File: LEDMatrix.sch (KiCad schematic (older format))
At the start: 71 parts

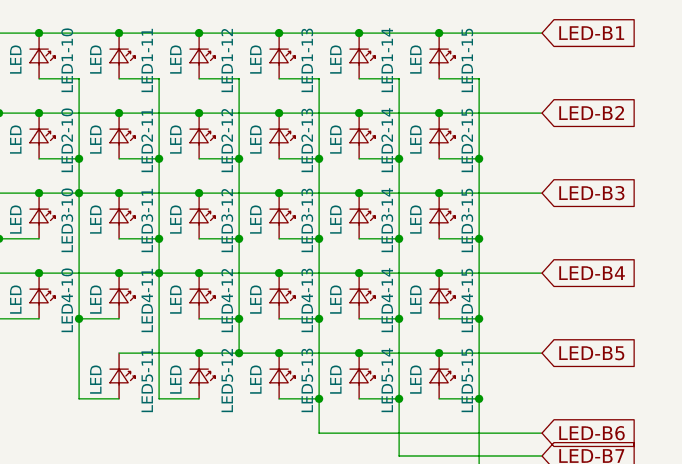
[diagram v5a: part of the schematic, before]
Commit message: Fix LED quantity for enter
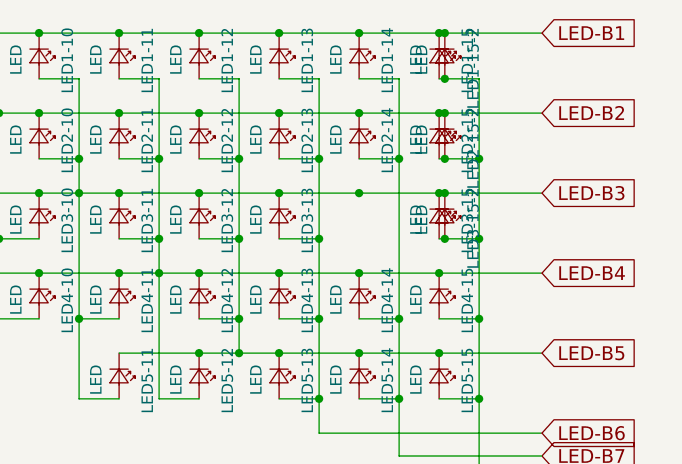
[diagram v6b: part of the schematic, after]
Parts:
- removed LED3-14: LED, MX_Alps_Hybrid:LED, symbol LED_Small
- added LED1-15-2, LED2-15-2, LED3-15-2: LED, MX_Alps_Hybrid:LED, symbol LED_Small
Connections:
- net LED-B1: now also LED1-15-2.1 (K)
- net LED-B2: now also LED2-15-2.1 (K)
- net LED-B3: now also LED3-15-2.1 (K)
- net LED-B8: now also LED1-15-2.2 (A), LED2-15-2.2 (A), LED3-15-2.2 (A)
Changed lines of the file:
@@
-$EndComp
-$Comp
-L LED_Small LED3-14
-U 1 1 5A6E13FF
-P 6950 2650
-F 0 "LED3-14" H 6825 2775 50  0000 L CNN
-F 1 "LED" H 6900 2550 50  0000 L CNN
-F 2 "MX_Alps_Hybrid:LED" V 6950 2650 50  0001 C CNN
-F 3 "" V 6950 2650 50  0001 C CNN
-	1    6950 2650
-	0    1    1    0
 $EndComp
 $Comp
@@
 Wire Wire Line
 	7125 2400 6950 2400
-Wire Wire Line
-	7125 2750 6950 2750
 Connection ~ 7125 2400
 Wire Wire Line
 	7125 3100 6950 3100
-Connection ~ 7125 2750
 Wire Wire Line
 	7125 3450 6950 3450
@@
 Connection ~ 4650 3250
 Connection ~ 4675 3450
+$Comp
+L LED_Small LED1-15-2
+U 1 1 5A6DC964
+P 7325 1950
+F 0 "LED1-15-2" H 7200 2075 50  0000 L CNN
+F 1 "LED" H 7275 1850 50  0000 L CNN
+F 2 "MX_Alps_Hybrid:LED" V 7325 1950 50  0001 C CNN
+F 3 "" V 7325 1950 50  0001 C CNN
+	1    7325 1950
+	0    1    1    0
+$EndComp
+Connection ~ 7325 1850
+Connection ~ 7325 2050
+$Comp
+L LED_Small LED2-15-2
+U 1 1 5A6DCCEC
+P 7325 2300
+F 0 "LED2-15-2" H 7200 2425 50  0000 L CNN
+F 1 "LED" H 7275 2200 50  0000 L CNN
+F 2 "MX_Alps_Hybrid:LED" V 7325 2300 50  0001 C CNN
+F 3 "" V 7325 2300 50  0001 C CNN
+	1    7325 2300
+	0    1    1    0
+$EndComp
+Connection ~ 7325 2200
+Connection ~ 7325 2400
+$Comp
+L LED_Small LED3-15-2
+U 1 1 5A6DD788
+P 7325 2650
+F 0 "LED3-15-2" H 7200 2775 50  0000 L CNN
+F 1 "LED" H 7275 2550 50  0000 L CNN
+F 2 "MX_Alps_Hybrid:LED" V 7325 2650 50  0001 C CNN
+F 3 "" V 7325 2650 50  0001 C CNN
+	1    7325 2650
+	0    1    1    0
+$EndComp
+Connection ~ 7325 2550
+Connection ~ 7325 2750
 $EndSCHEMATC

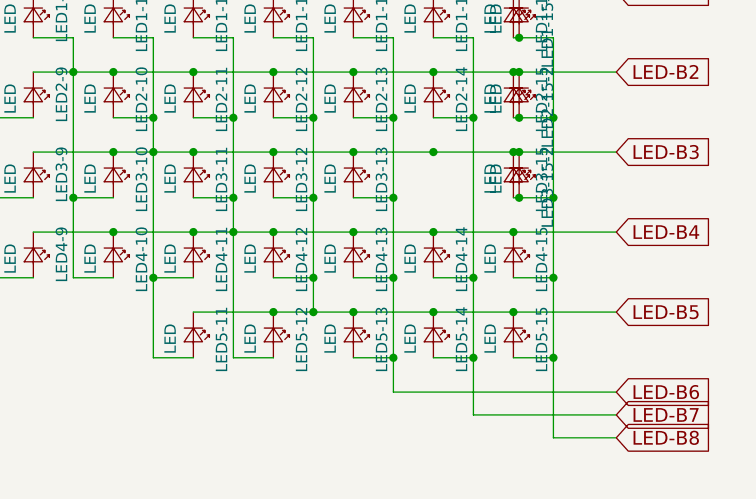
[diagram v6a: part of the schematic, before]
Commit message: Add missing shift-row footprints
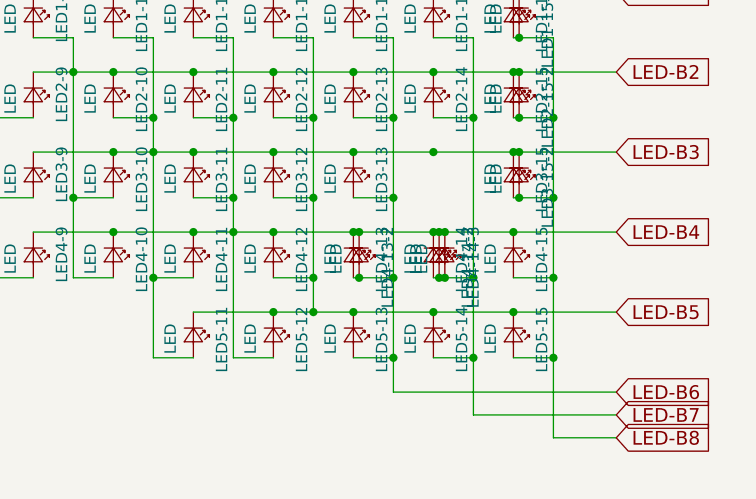
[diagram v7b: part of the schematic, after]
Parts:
- added LED4-13-2, LED4-14-2: LED, MX_Alps_Hybrid:LED, symbol LED_Small
- added LED4-14-3: LED, MX_Alps_Hybrid:LED-FLIPPED, symbol LED_Small
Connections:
- net LED-B4: now also LED4-13-2.1 (K), LED4-14-2.1 (K), LED4-14-3.1 (K)
- net LED-B6: now also LED4-13-2.2 (A)
- net LED-B7: now also LED4-14-2.2 (A), LED4-14-3.2 (A)
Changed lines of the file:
@@
 Connection ~ 7325 2550
 Connection ~ 7325 2750
+$Comp
+L LED_Small LED4-13-2
+U 1 1 5A6DE057
+P 6625 3000
+F 0 "LED4-13-2" H 6500 3125 50  0000 L CNN
+F 1 "LED" H 6575 2900 50  0000 L CNN
+F 2 "MX_Alps_Hybrid:LED" V 6625 3000 50  0001 C CNN
+F 3 "" V 6625 3000 50  0001 C CNN
+	1    6625 3000
+	0    1    1    0
+$EndComp
+Connection ~ 6625 2900
+Connection ~ 6625 3100
+$Comp
+L LED_Small LED4-14-2
+U 1 1 5A6DEC93
+P 6975 3000
+F 0 "LED4-14-2" H 6850 3125 50  0000 L CNN
+F 1 "LED" H 6925 2900 50  0000 L CNN
+F 2 "MX_Alps_Hybrid:LED" V 6975 3000 50  0001 C CNN
+F 3 "" V 6975 3000 50  0001 C CNN
+	1    6975 3000
+	0    1    1    0
+$EndComp
+$Comp
+L LED_Small LED4-14-3
+U 1 1 5A6DEEC6
+P 7000 3000
+F 0 "LED4-14-3" H 6875 3125 50  0000 L CNN
+F 1 "LED" H 6950 2900 50  0000 L CNN
+F 2 "MX_Alps_Hybrid:LED-FLIPPED" V 7000 3000 50  0001 C CNN
+F 3 "" V 7000 3000 50  0001 C CNN
+	1    7000 3000
+	0    1    1    0
+$EndComp
+Connection ~ 6975 2900
+Connection ~ 7000 2900
+Connection ~ 7000 3100
+Connection ~ 6975 3100
 $EndSCHEMATC

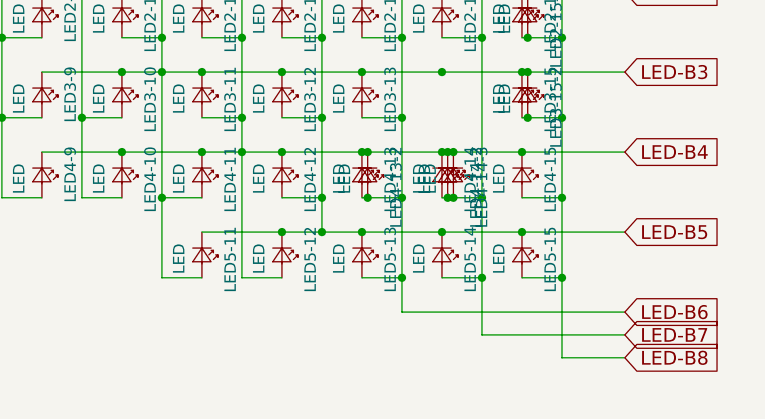
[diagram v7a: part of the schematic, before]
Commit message: Finish placing LEDs
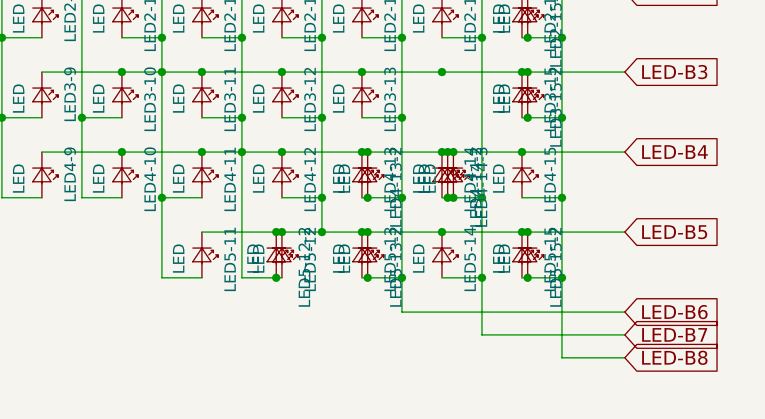
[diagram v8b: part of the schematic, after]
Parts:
- added LED5-12-2, LED5-15-2: LED, MX_Alps_Hybrid:LED-FLIPPED, symbol LED_Small
- added LED5-13-2: LED, MX_Alps_Hybrid:LED, symbol LED_Small
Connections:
- net LED-B4: now also LED5-12-2.2 (A)
- net LED-B5: now also LED5-12-2.1 (K), LED5-13-2.1 (K), LED5-15-2.1 (K)
- net LED-B6: now also LED5-13-2.2 (A)
- net LED-B8: now also LED5-15-2.2 (A)
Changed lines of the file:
@@
 Connection ~ 7000 3100
 Connection ~ 6975 3100
+$Comp
+L LED_Small LED5-12-2
+U 1 1 5A6E01FE
+P 6225 3350
+F 0 "LED5-12-2" H 6100 3475 50  0000 L CNN
+F 1 "LED" H 6175 3250 50  0000 L CNN
+F 2 "MX_Alps_Hybrid:LED-FLIPPED" V 6225 3350 50  0001 C CNN
+F 3 "" V 6225 3350 50  0001 C CNN
+	1    6225 3350
+	0    1    1    0
+$EndComp
+$Comp
+L LED_Small LED5-13-2
+U 1 1 5A6E02F3
+P 6625 3350
+F 0 "LED5-13-2" H 6500 3475 50  0000 L CNN
+F 1 "LED" H 6575 3250 50  0000 L CNN
+F 2 "MX_Alps_Hybrid:LED" V 6625 3350 50  0001 C CNN
+F 3 "" V 6625 3350 50  0001 C CNN
+	1    6625 3350
+	0    1    1    0
+$EndComp
+$Comp
+L LED_Small LED5-15-2
+U 1 1 5A6E1059
+P 7325 3350
+F 0 "LED5-15-2" H 7200 3475 50  0000 L CNN
+F 1 "LED" H 7275 3250 50  0000 L CNN
+F 2 "MX_Alps_Hybrid:LED-FLIPPED" V 7325 3350 50  0001 C CNN
+F 3 "" V 7325 3350 50  0001 C CNN
+	1    7325 3350
+	0    1    1    0
+$EndComp
+Connection ~ 6225 3250
+Connection ~ 6225 3450
+Connection ~ 6625 3250
+Connection ~ 6625 3450
+Connection ~ 7325 3450
+Connection ~ 7325 3250
 $EndSCHEMATC
